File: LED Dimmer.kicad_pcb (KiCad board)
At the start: 2 copper layers, 78 parts, among them P1 Red Load, P2 Green Load, P3 Blue Load, P4 PWR, Q1 TIP31C, Q2 TIP31C, Q3 TIP31C, Q4 Q_PNP_EBC, Q5 Q_PNP_EBC, Q6 Q_NPN_EBC, SW1 SW_SPDT, SW10 SW_SPDT, SW11 SW_SPDT, SW12 SW_SPDT, SW2 SW_SPDT, SW3 SW_SPDT, SW4 SW_SPDT, SW5 SW_SPDT, SW6 SW_SPDT, SW7 SW_SPDT, SW8 SW_SPDT, SW9 SW_SPDT, U1 LM358, U2 LM358, U3 LM358, U4 LM555N

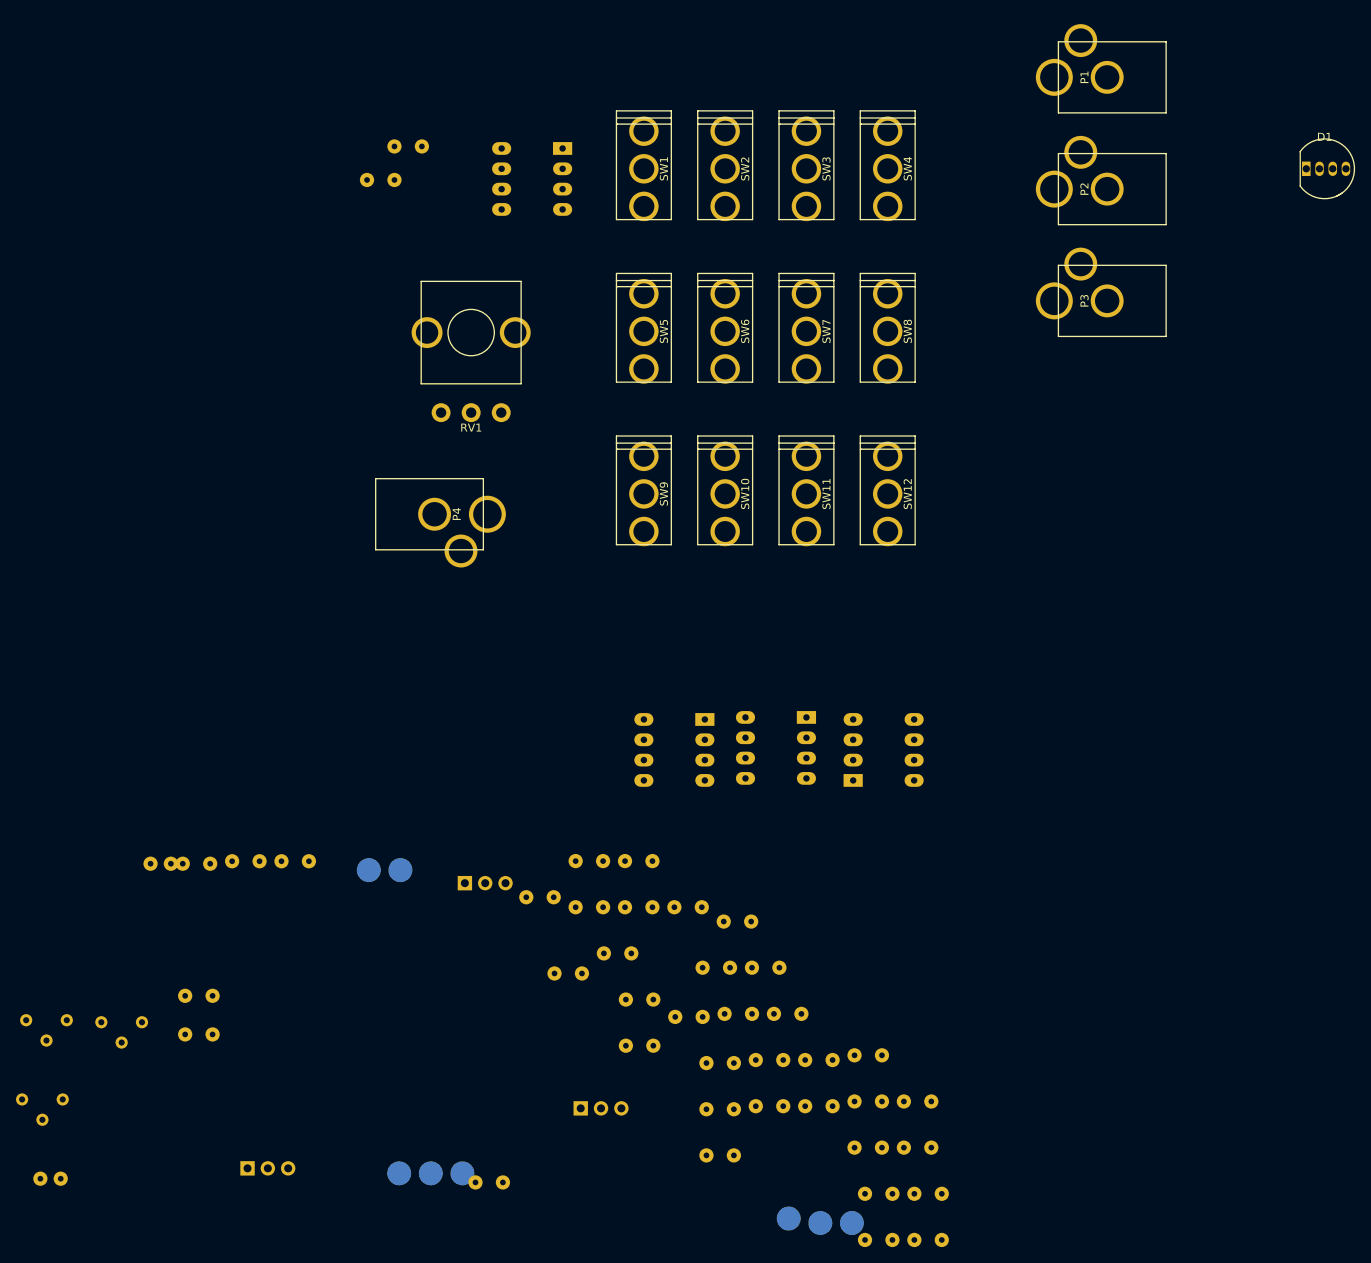
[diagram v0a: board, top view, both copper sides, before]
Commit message: Components placed, edge cuts marked, ready for routing
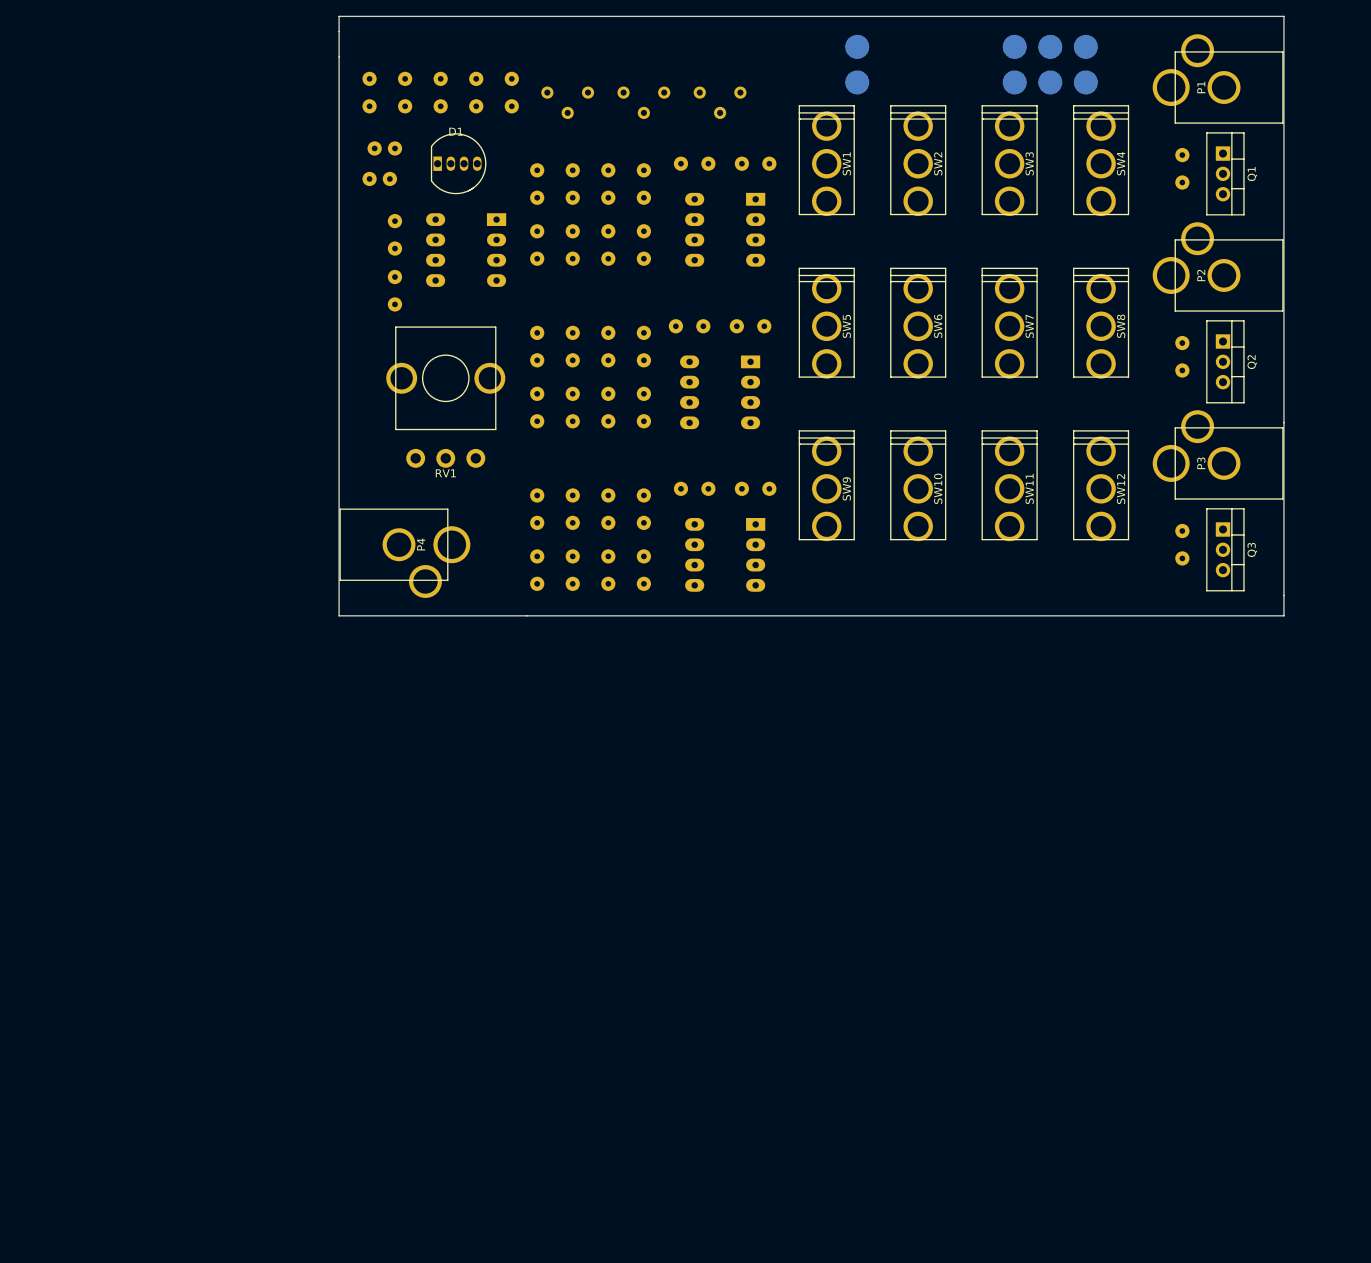
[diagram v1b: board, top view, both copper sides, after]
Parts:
- Q1, Q2, Q3: moved to F.Cu
- moved Q1 176.0 mm to (198.1, 64.1), turned to 270 degrees
- moved TP1 161.1 mm to (181.0, 55.2)
- moved TP6 158.6 mm to (172.1, 50.8)
- moved Q4 151.7 mm to (132.7, 56.5)
- moved TP7 149.2 mm to (152.4, 50.8)
- moved TP2 145.7 mm to (176.5, 55.2)
- moved TP3 144.0 mm to (172.1, 55.2)
- moved TP8 142.6 mm to (152.4, 55.2)
- moved R39 138.8 mm to (95.9, 56.5), turned to 90 degrees
- moved TP4 136.5 mm to (181.0, 50.8)
- moved C1 136.2 mm to (94.6, 63.5), turned to 180 degrees
- moved Q5 133.3 mm to (123.2, 56.5)
- moved Q6 133.0 mm to (113.7, 56.5)
- moved R1 131.1 mm to (125.7, 67.9), turned to 90 degrees
- moved TP5 131.1 mm to (176.5, 50.8)
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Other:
- board outline added: 118.1 x 74.9 mm
- net class Default: clearance 0.2 -> 0.254; trace_width 0.25 -> 0.254; via_drill 0.4 -> 0.4064
- net class PWR added: clearance 0.381, trace_width 0.508, via_dia 0.6, via_drill 0.4064
- rule trace_clearance: 0.2 -> 0.254
- rule trace_min: 0.2 -> 0.254
- rule via_min_size: 0.4 -> 0.4064
- board text added: "B"
- board text added: "G"
- board text added: "KNOB OUT"
- board text added: "LAMBDA WAVE"
- board text added: "PWM SIGNAL"
- board text added: "R"
- board text added: "SWITCH OUTPUT"

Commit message: Routed
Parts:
- TP1, TP2, TP3, TP4, TP5, TP6, TP7, TP8: footprint LED Dimmer Footprints:Measurement_Point_Round-SMD-Pad_Big -> LED Dimmer Footprints:test_pt_alt
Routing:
- net +12V: track 0.00 -> 366.0 mm, vias 0 -> 1
- net GND: track 0.00 -> 335.4 mm
- net LEDB: track 0.00 -> 148.6 mm
- net +6V: track 0.00 -> 143.0 mm
- net LEDG: track 0.00 -> 135.2 mm
- net LAMBDA: track 0.00 -> 134.3 mm
- net LEDR: track 0.00 -> 107.4 mm
- net VB: track 0.00 -> 79.9 mm
- net VG: track 0.00 -> 78.8 mm, vias 0 -> 1
- net Net-(Q3-Pad1): track 0.00 -> 76.1 mm
- net Net-(Q2-Pad1): track 0.00 -> 75.1 mm
- net Net-(Q1-Pad1): track 0.00 -> 73.1 mm
- net Net-(R14-Pad2): track 0.00 -> 73.0 mm
- net Net-(R22-Pad2): track 0.00 -> 73.0 mm
- net Net-(R6-Pad2): track 0.00 -> 72.3 mm
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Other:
- net class Default: clearance 0.254 -> 0.4572
- net class PWR: clearance 0.381 -> 0.4572
- rule trace_clearance: 0.254 -> 0.4572
- board text added: "RABG"

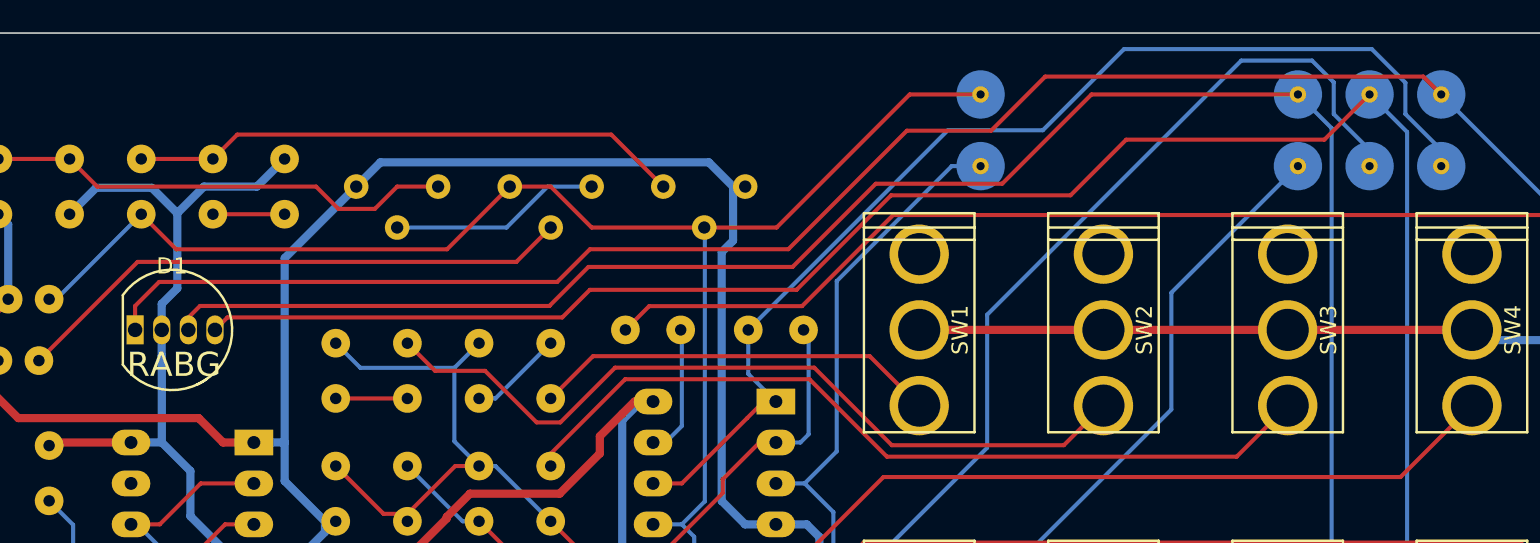
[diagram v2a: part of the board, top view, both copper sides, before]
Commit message: Nudged RGB LED to line up with knob; added front panel (without silks)
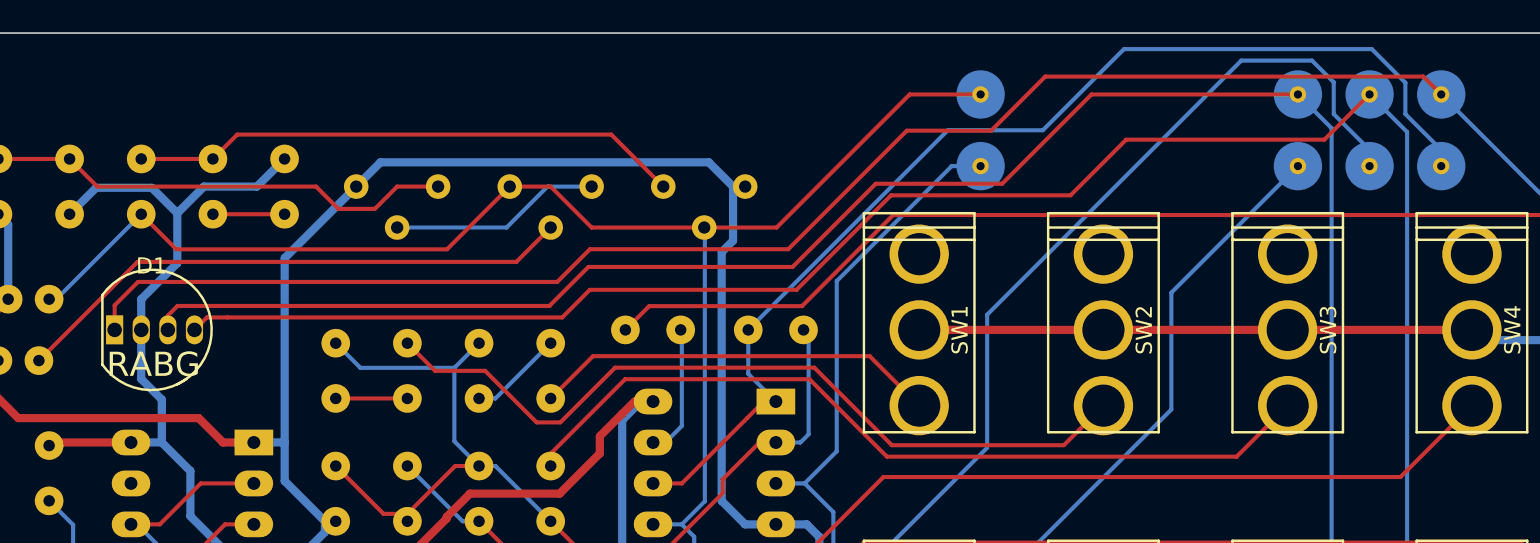
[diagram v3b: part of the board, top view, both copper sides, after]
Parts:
- moved D1 1.27 mm to (101.0, 65.4)
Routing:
- net LEDB: track 148.6 -> 150.0 mm
- net LEDR: track 107.4 -> 108.7 mm
- net LEDG: track 135.2 -> 136.5 mm
- net +12V: track 366.0 -> 367.1 mm

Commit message: Renamed library for compatibility with 3D viewer
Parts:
- C1: footprint LED Dimmer Footprints:C_Disc -> led_dimmer_footprints:C_Disc
- D1: footprint LED Dimmer Footprints:LED_D5.0mm-4 -> led_dimmer_footprints:LED_D5.0mm-4
- D2: footprint LED Dimmer Footprints:D_axial -> led_dimmer_footprints:D_axial
- P1, P2, P3, P4: footprint LED Dimmer Footprints:2.1ID_5.5OD_SIDE_MOUNT_JACK -> led_dimmer_footprints:2.1ID_5.5OD_SIDE_MOUNT_JACK
- Q1, Q2, Q3: footprint LED Dimmer Footprints:TO-220_Vertical -> led_dimmer_footprints:TO-220_Vertical
- Q4, Q5, Q6: footprint LED Dimmer Footprints:TO-92_Molded_Wide -> led_dimmer_footprints:TO-92_Molded_Wide
- R1, R10, R11, R12, R13, R14, R15, R16, R17, R18, R19, R2, R20, R21, R22, R23, R24, R25, R26, R27, R28, R29, R3, R30, R31, R32, R33, R34, R35, R36, R37, R38, R39, R4, R40, R5, R6, R7, R8, R9: footprint LED Dimmer Footprints:R_Axial -> led_dimmer_footprints:R_Axial
- RV1: footprint LED Dimmer Footprints:POT_UM_296RE -> led_dimmer_footprints:POT_UM_296RE
- SW1, SW10, SW11, SW12, SW2, SW3, SW4, SW5, SW6, SW7, SW8, SW9: footprint LED Dimmer Footprints:SW_SPDT_PCBPM -> led_dimmer_footprints:SW_SPDT_PCBPM
- TP1, TP2, TP3, TP4, TP5, TP6, TP7, TP8: footprint LED Dimmer Footprints:test_pt_alt -> led_dimmer_footprints:test_pt_alt
- U1, U2, U3: footprint LED Dimmer Footprints:DIP8_dualopamp -> led_dimmer_footprints:DIP8_dualopamp
- U4: footprint LED Dimmer Footprints:DIP8 -> led_dimmer_footprints:DIP8

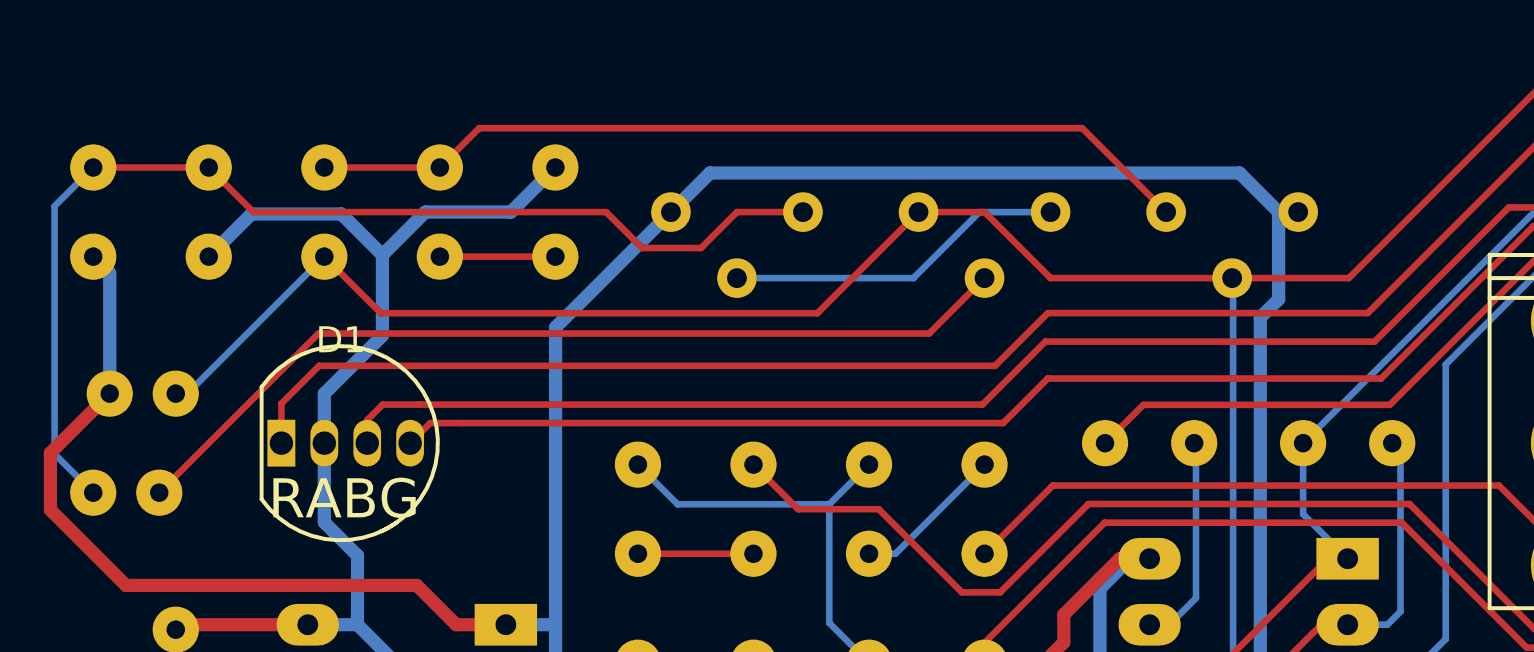
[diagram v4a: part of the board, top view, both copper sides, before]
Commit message: Rerouted around TO-92 footprints (in the last commit I grew the pads on TO-92 footprint but forgot to mention it)
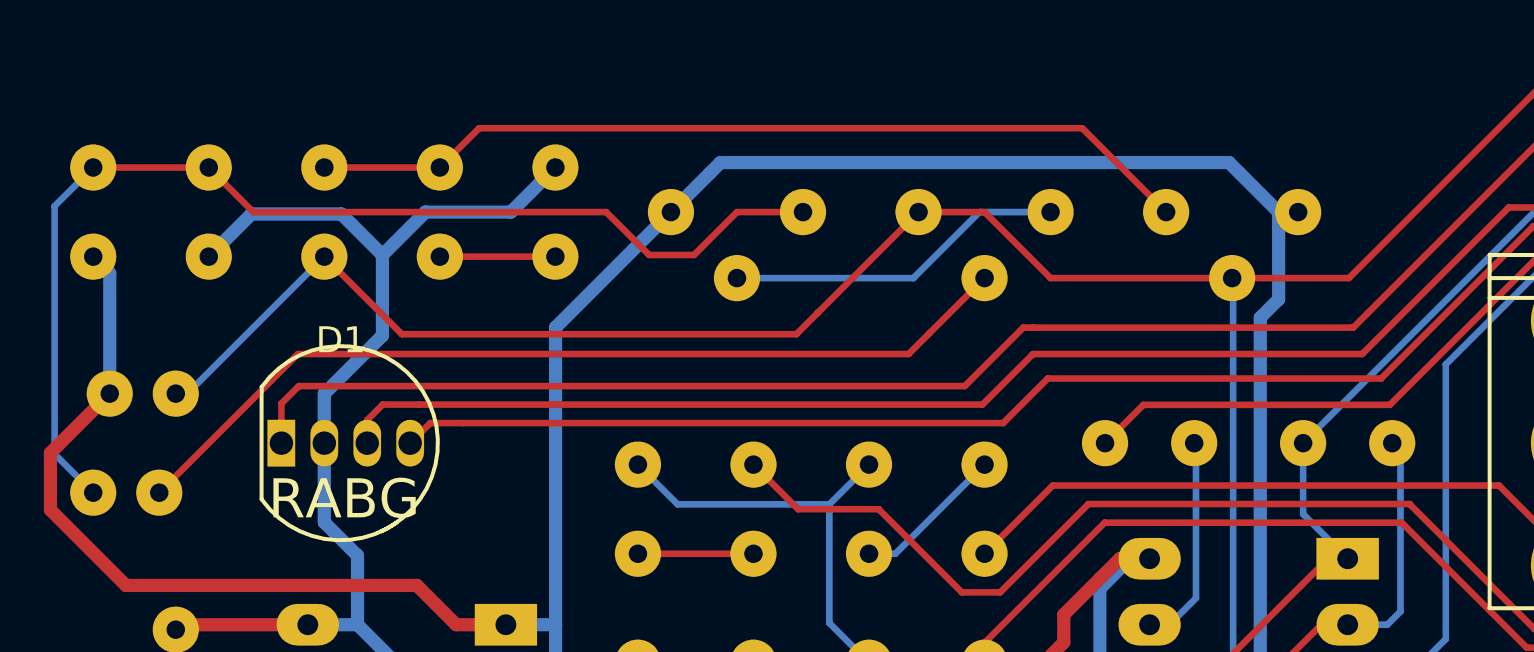
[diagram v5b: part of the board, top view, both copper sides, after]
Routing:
- net LAMBDA: track 134.3 -> 135.0 mm
